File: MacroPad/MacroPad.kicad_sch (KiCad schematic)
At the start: 27 parts, among them SW1 CherryMX, SW10 CherryMX, SW11 CherryMX, SW12 CherryMX, SW2 CherryMX, SW3 CherryMX, SW4 CherryMX, SW5 CherryMX, SW6 CherryMX, SW7 CherryMX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

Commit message: Finished PCB i think
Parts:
- removed SW11: CherryMX, Switch_Keyboard_Cherry_MX:SW_Cherry_MX_Plate_1.00u, symbol CherryMX:CherryMX
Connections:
- net GND: now also U1.38 (GND)
- net SW4: now also U1.12 (MTMS/GPIO14/ADC2_CH6); no longer U1.10 (DAC_2/ADC2_CH9/GPIO26)
- net SW6: now also U1.10 (DAC_2/ADC2_CH9/GPIO26); no longer U1.12 (MTMS/GPIO14/ADC2_CH6)
- no-connect marks 24 -> 23
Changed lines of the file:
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@@
   (no_connect (at 274.32 62.23))
   (no_connect (at 274.32 57.15))
-  (no_connect (at 274.32 26.67))
   (no_connect (at 104.14 33.02))
   (no_connect (at 205.74 64.77))
@@
     (stroke (width 0) (type default) (color 0 0 0 0))
   )
+  (wire (pts (xy 274.32 26.67) (xy 283.21 26.67))
+    (stroke (width 0) (type default) (color 0 0 0 0))
+  )
   (polyline (pts (xy 123.19 20.32) (xy 123.19 135.89))
     (stroke (width 0) (type default) (color 0 0 0 0))
@@
   )
   (wire (pts (xy 96.52 81.28) (xy 109.22 81.28))
+    (stroke (width 0) (type default) (color 0 0 0 0))
+  )
+  (wire (pts (xy 283.21 26.67) (xy 283.21 29.21))
     (stroke (width 0) (type default) (color 0 0 0 0))
   )
@@
     )
   )
-  (global_label "SW6" (shape input) (at 205.74 54.61 180) (fields_autoplaced)
-    (effects (font (size 1.27 1.27)) (justify right))
-    (property "Intersheet References" "${INTERSHEET_REFS}" (id 0) (at 199.4564 54.5306 0)
+  (global_label "SW6" (shape input) (at 205.74 49.53 180) (fields_autoplaced)
+    (effects (font (size 1.27 1.27)) (justify right))
+    (property "Intersheet References" "${INTERSHEET_REFS}" (id 0) (at 199.4564 49.4506 0)
       (effects (font (size 1.27 1.27)) (justify right) hide)
     )
@@
     )
   )
-  (global_label "SW4" (shape input) (at 205.74 49.53 180) (fields_autoplaced)
-    (effects (font (size 1.27 1.27)) (justify right))
-    (property "Intersheet References" "${INTERSHEET_REFS}" (id 0) (at 199.4564 49.4506 0)
+  (global_label "SW4" (shape input) (at 205.74 54.61 180) (fields_autoplaced)
+    (effects (font (size 1.27 1.27)) (justify right))
+    (property "Intersheet References" "${INTERSHEET_REFS}" (id 0) (at 199.4564 54.5306 0)
       (effects (font (size 1.27 1.27)) (justify right) hide)
     )
@@
     )
     (property "Datasheet" "" (id 3) (at 44.45 40.64 0)
+      (effects (font (size 1.27 1.27)) hide)
+    )
+    (pin "1")
+  )
+  (symbol (lib_id "power:GND") (at 283.21 29.21 0) (unit 1)
+    (in_bom yes) (on_board yes) (fields_autoplaced)
+    (property "Reference" "#PWR?" (id 0) (at 283.21 35.56 0)
+      (effects (font (size 1.27 1.27)) hide)
+    )
+    (property "Value" "GND" (id 1) (at 283.21 34.29 0))
+    (property "Footprint" "" (id 2) (at 283.21 29.21 0)
+      (effects (font (size 1.27 1.27)) hide)
+    )
+    (property "Datasheet" "" (id 3) (at 283.21 29.21 0)
       (effects (font (size 1.27 1.27)) hide)
     )
@@
     (pin "1")
   )
-  (symbol (lib_id "CherryMX:CherryMX") (at 63.5 186.69 0) (unit 1)
-    (in_bom yes) (on_board yes) (fields_autoplaced)
-    (property "Reference" "SW11" (id 0) (at 63.5 179.07 0))
-    (property "Value" "CherryMX" (id 1) (at 63.5 181.61 0))
-    (property "Footprint" "Switch_Keyboard_Cherry_MX:SW_Cherry_MX_Plate_1.00u" (id 2) (at 63.5 186.055 0)
-      (effects (font (size 1.27 1.27)) hide)
-    )
-    (property "Datasheet" "" (id 3) (at 63.5 186.055 0)
-      (effects (font (size 1.27 1.27)) hide)
-    )
-    (pin "1")
-    (pin "2")
-  )
   (symbol (lib_id "CherryMX:CherryMX") (at 35.56 165.1 0) (unit 1)
     (in_bom yes) (on_board yes) (fields_autoplaced)
@@
       (reference "#PWR0126") (unit 1) (value "GND") (footprint "")
     )
+    (path "/34e41f35-7545-4f1a-8fb0-63e57b3abf99"
+      (reference "#PWR?") (unit 1) (value "GND") (footprint "")
+    )
     (path "/f46ec625-5522-41cc-be5f-679b6d2d5d61"
       (reference "C1") (unit 1) (value "10u") (footprint "Capacitor_SMD:C_1206_3216Metric_Pad1.33x1.80mm_HandSolder")
@@
       (reference "SW10") (unit 1) (value "CherryMX") (footprint "Switch_Keyboard_Cherry_MX:SW_Cherry_MX_Plate_1.00u")
     )
-    (path "/d0c21061-7bdc-4398-929e-fd92796a2721"
-      (reference "SW11") (unit 1) (value "CherryMX") (footprint "Switch_Keyboard_Cherry_MX:SW_Cherry_MX_Plate_1.00u")
-    )
     (path "/ca7e6571-12e2-46a7-8a55-d805e55d7c13"

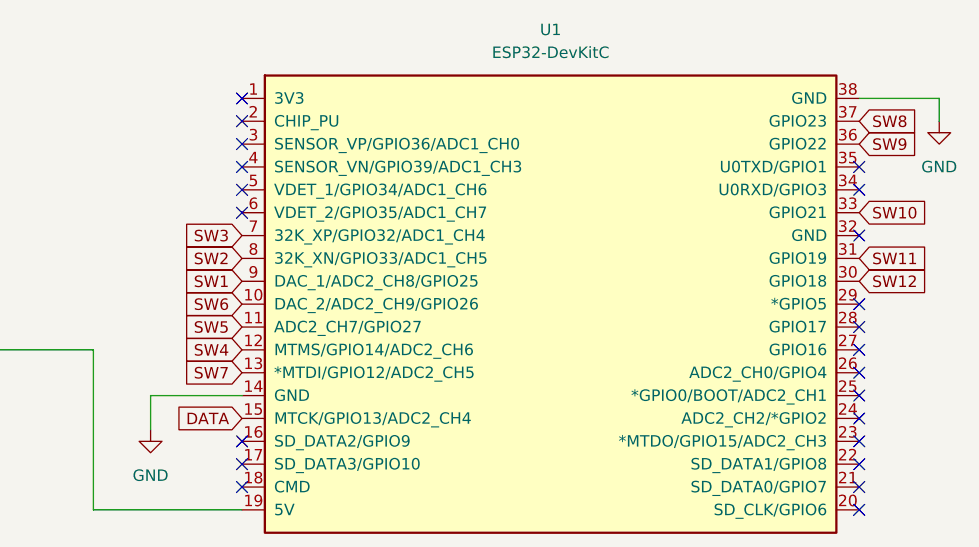
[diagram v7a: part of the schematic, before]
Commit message: updated PCB (esp at top now)
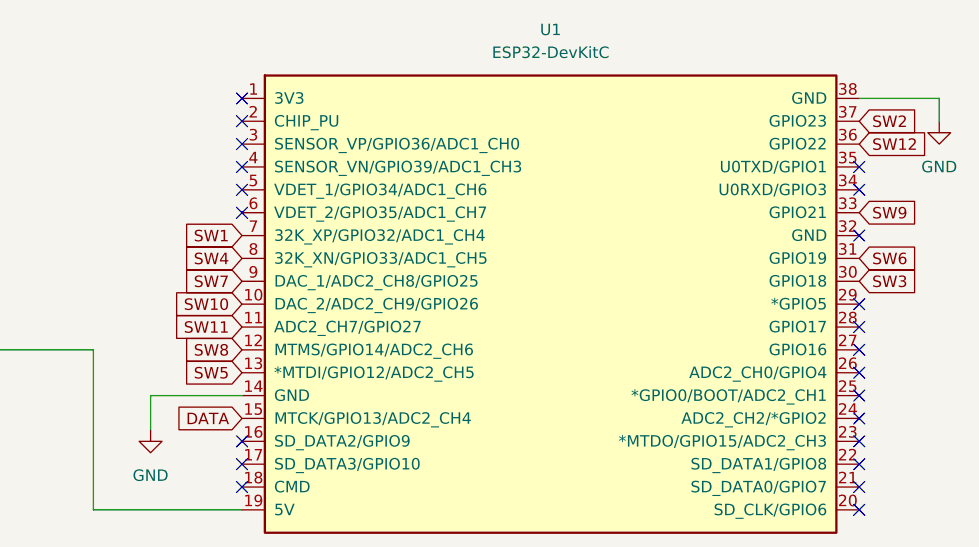
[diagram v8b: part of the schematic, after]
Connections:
- net SW1: now also U1.7 (32K_XP/GPIO32/ADC1_CH4); no longer U1.9 (DAC_1/ADC2_CH8/GPIO25)
- net SW10: now also U1.10 (DAC_2/ADC2_CH9/GPIO26); no longer U1.33 (GPIO21)
- net SW11: now also U1.11 (ADC2_CH7/GPIO27); no longer U1.31 (GPIO19)
- net SW12: now also U1.36 (GPIO22); no longer U1.30 (GPIO18)
- net SW2: now also U1.37 (GPIO23); no longer U1.8 (32K_XN/GPIO33/ADC1_CH5)
- net SW3: now also U1.30 (GPIO18); no longer U1.7 (32K_XP/GPIO32/ADC1_CH4)
- net SW4: now also U1.8 (32K_XN/GPIO33/ADC1_CH5); no longer U1.12 (MTMS/GPIO14/ADC2_CH6)
- net SW5: now also U1.13 (*MTDI/GPIO12/ADC2_CH5); no longer U1.11 (ADC2_CH7/GPIO27)
- net SW6: now also U1.31 (GPIO19); no longer U1.10 (DAC_2/ADC2_CH9/GPIO26)
- net SW7: now also U1.9 (DAC_1/ADC2_CH8/GPIO25); no longer U1.13 (*MTDI/GPIO12/ADC2_CH5)
- net SW8: now also U1.12 (MTMS/GPIO14/ADC2_CH6); no longer U1.37 (GPIO23)
- net SW9: now also U1.33 (GPIO21); no longer U1.36 (GPIO22)
